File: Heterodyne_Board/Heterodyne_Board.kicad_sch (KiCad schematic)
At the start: 67 parts, among them J1 Barrel_Jack, J2 SWITCH, J3 LED, J4 AudioJack2_Ground_Switch, J5 Speaker, J6 Microphone, J7 AVR-ISP-6, J8 AVR-ISP-6, SW1 SW_SPST, SW2 SW_SPST, SW3 SW_SPST, U1 AP2112K-3.3, U2 LM386, U3 TLV9054xD, U4 ATtiny85-20P, U5 TS5A3159DCK, U6 W25X40CLSN

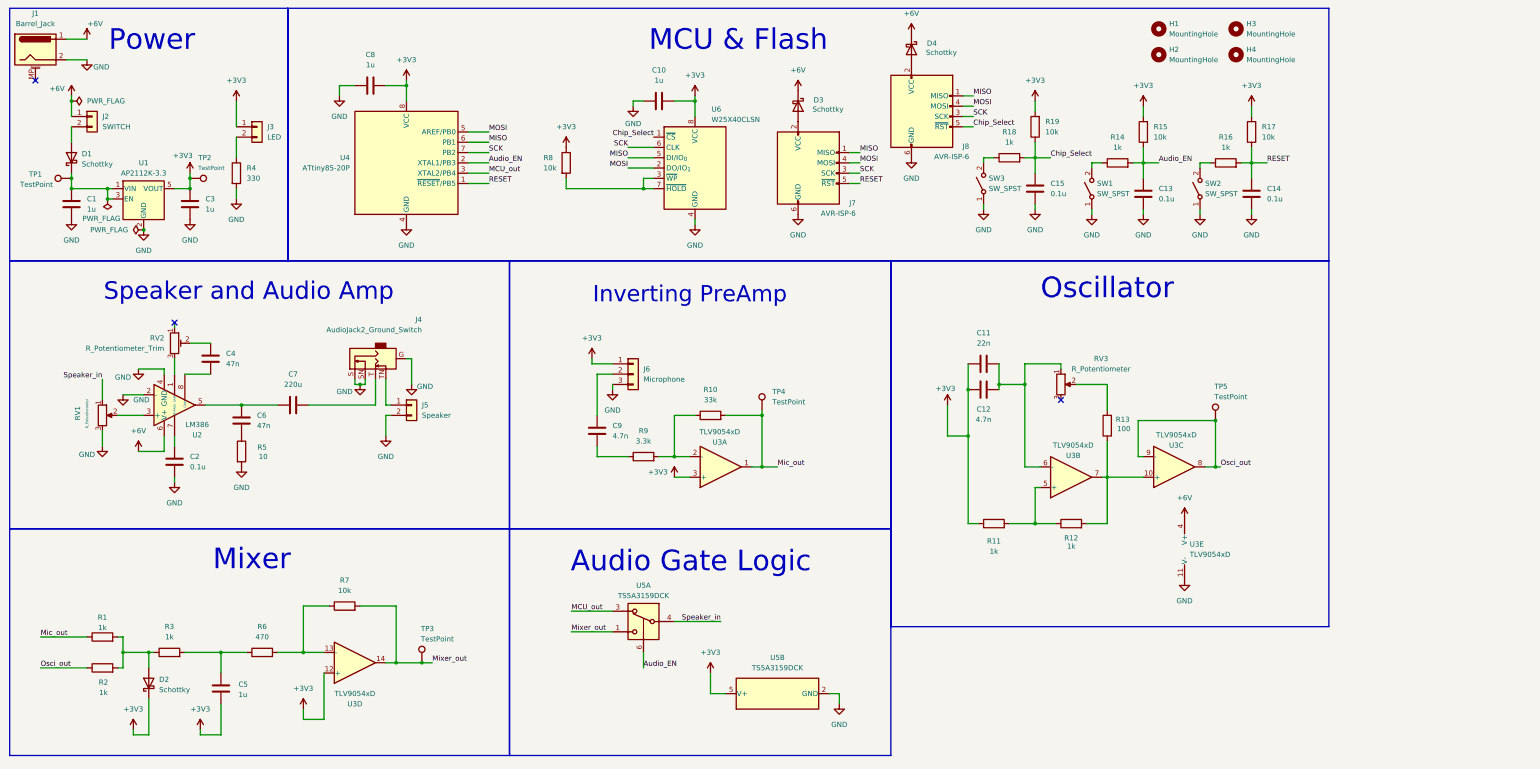
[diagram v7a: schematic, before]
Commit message: updated board with mcu flash fixes
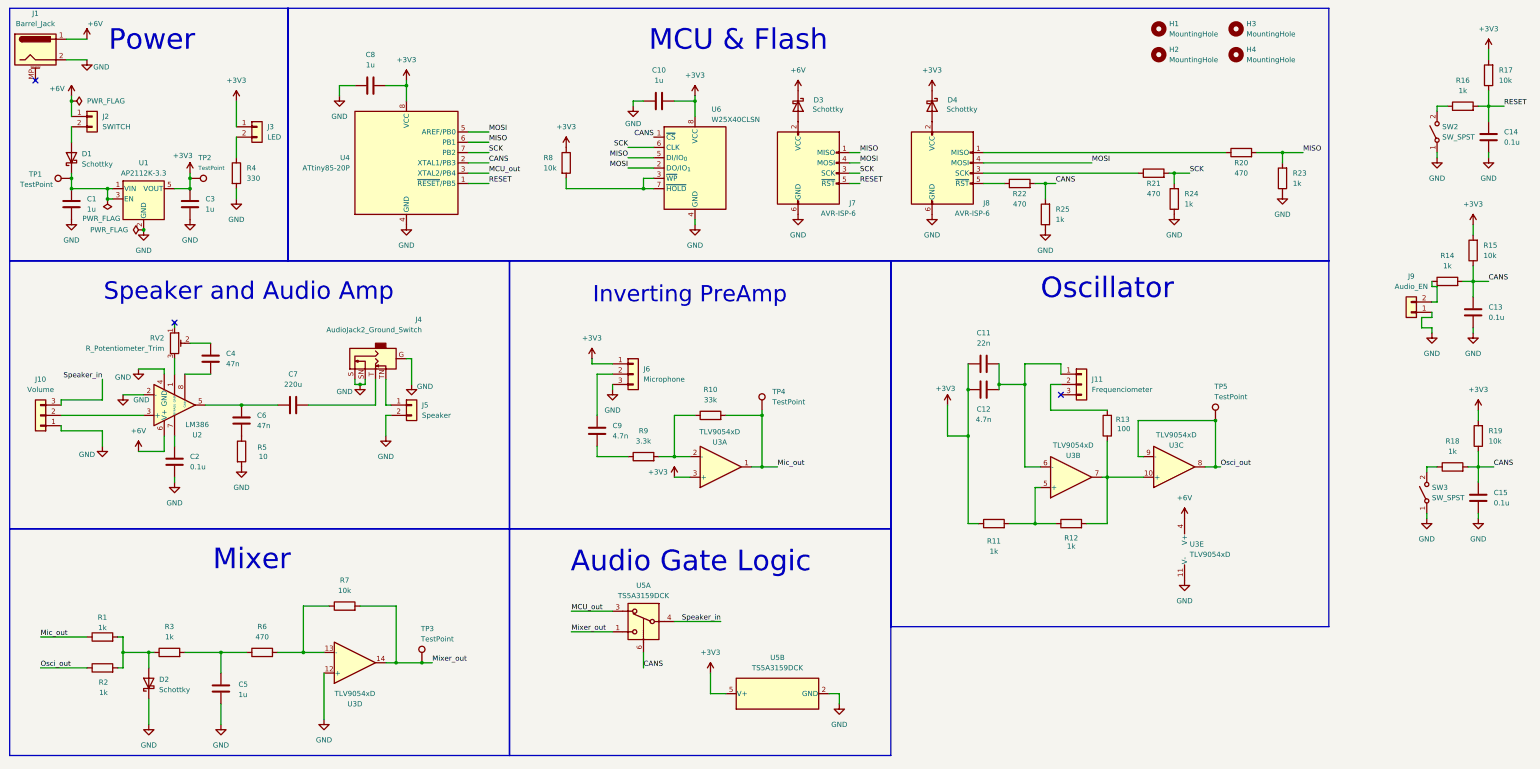
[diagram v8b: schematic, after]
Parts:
- removed RV1, RV3: R_Potentiometer, Potentiometer_THT:Potentiometer_Bourns_PTV09A-1_Single_Vertical, symbol Device:R_Potentiometer
- removed SW1: SW_SPST, Button_Switch_THT:SW_PUSH_6mm_H5mm, symbol Switch:SW_SPST
- added J10: Volume, Connector_Molex:Molex_KK-254_AE-6410-03A_1x03_P2.54mm_Vertical, symbol Connector_Generic:Conn_01x03
- added J11: Frequenciometer, Connector_Molex:Molex_KK-254_AE-6410-03A_1x03_P2.54mm_Vertical, symbol Connector_Generic:Conn_01x03
- added J9: Audio_EN, Connector_Molex:Molex_KK-254_AE-6410-02A_1x02_P2.54mm_Vertical, symbol Connector_Generic:Conn_01x02
- added R20, R21, R22: 470, symbol Device:R
- added R23, R24, R25: 1k, symbol Device:R
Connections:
- net +3V3: now also D4.1 (K); no longer C5.2, D2.1 (K), U3.12 (+)
- net +6V: no longer D4.1 (K)
- net GND: now also C5.2, D2.1 (K), U3.12 (+), J10.1 (Pin_1), J9.1 (Pin_1), R23.1, R24.1, R25.1
- net MISO: now also R20.2, R23.2; no longer J8.1 (MISO)
- net SCK: now also R21.2, R24.2; no longer J8.3 (SCK)
- net Speaker_in: now also J10.3 (Pin_3)
- net at C11.2, C12.2, U3.6 (-): now also J11.1 (Pin_1)
- net at R13.2: now also J11.2 (Pin_2)
- net at R14.1: now also J9.2 (Pin_2)
- net at U2.3 (+): now also J10.2 (Pin_2)
- net Audio_EN renamed CANS
- net CANS: now also C15.2, R18.2, R19.1, U6.1 (~{CS}), R22.2, R25.2
- removed net Chip_Select: C15.2, J8.5 (~{RST}), R18.2, R19.1, U6.1 (~{CS})
- new net: J8.3 (SCK), R21.1
- new net: J8.1 (MISO), R20.1
- new net: J8.5 (~{RST}), R22.1
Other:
- moved on the sheet: C13, C14, C15, D4, J8, R14, R15, R16, R17, R18, R19, SW2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
